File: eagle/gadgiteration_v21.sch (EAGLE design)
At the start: 56 parts, among them IC1 ATMEGA168P, J1 2.1MMJACK, U2 TPA2005D1DGNRQ1, X1 16.00MHz

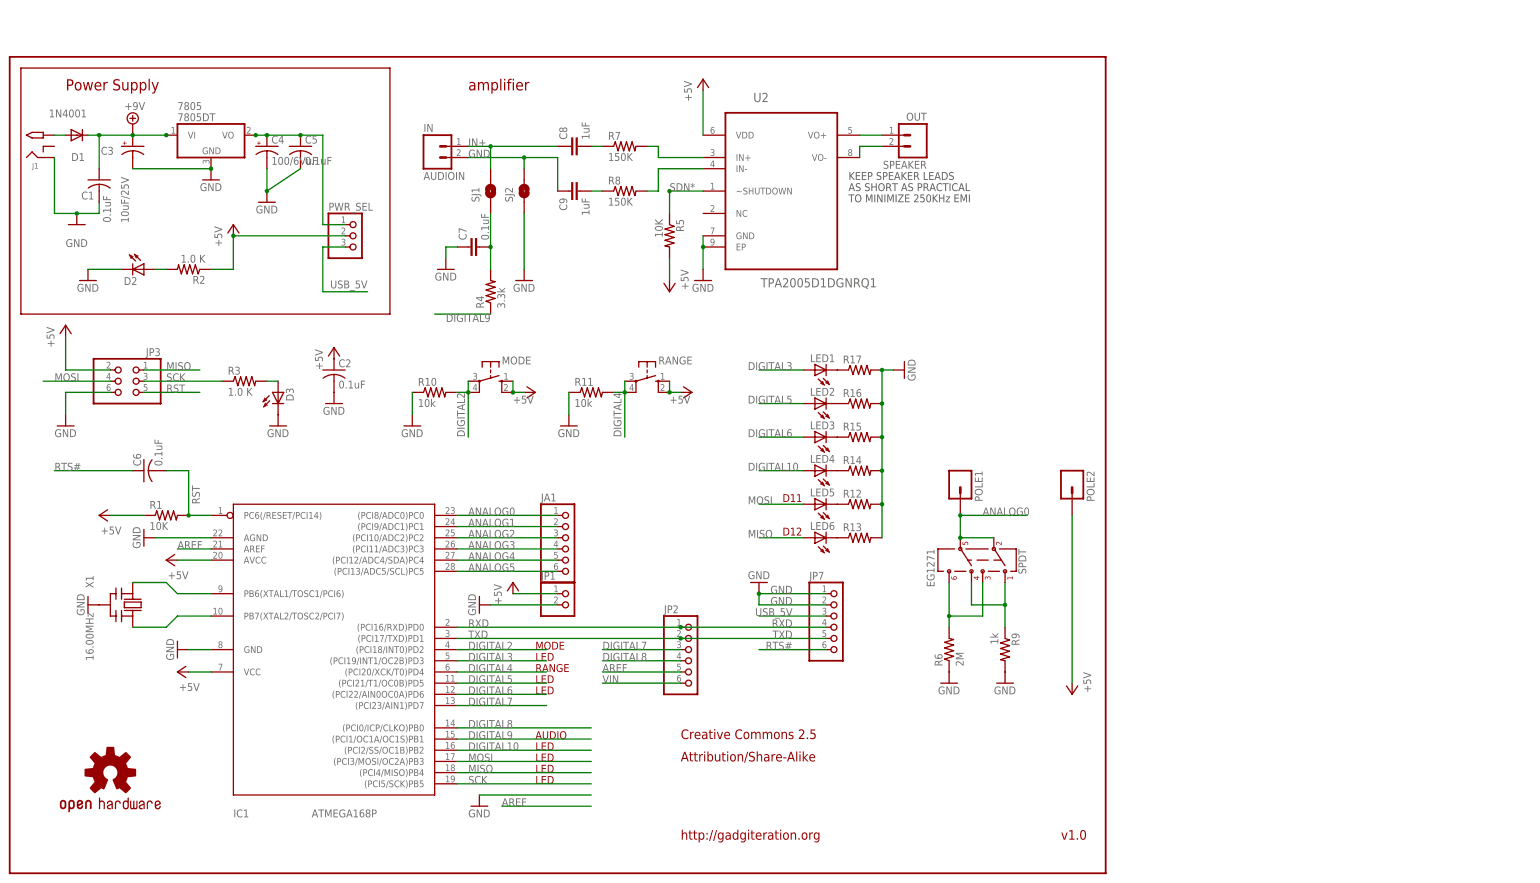
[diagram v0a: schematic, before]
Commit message: added v21 files, including readme and eagle files
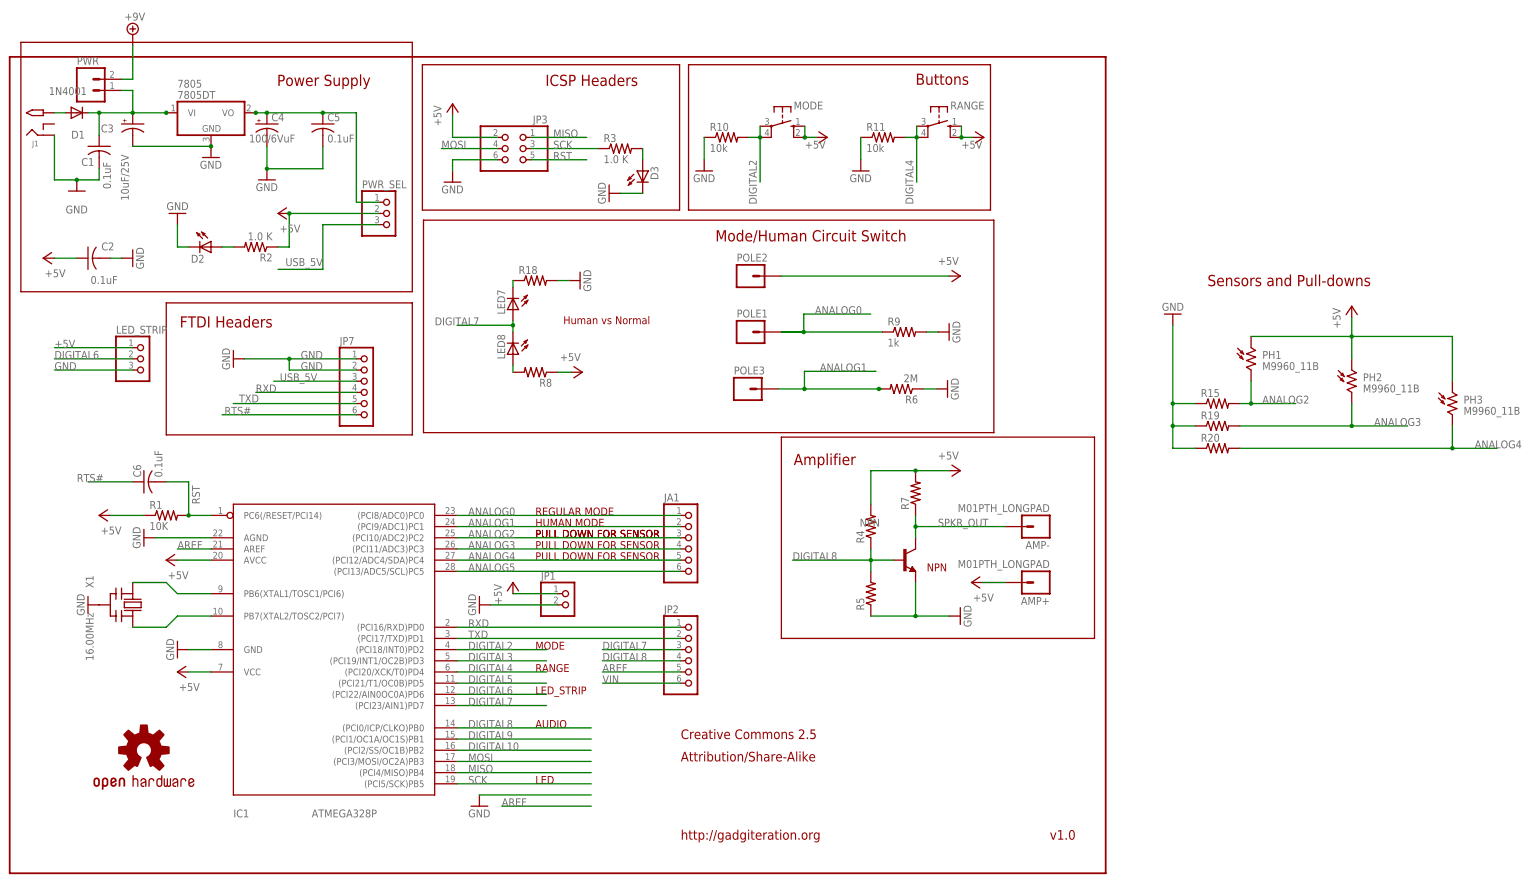
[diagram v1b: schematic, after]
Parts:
- removed AUDIOIN: IN, SparkFun:M02PTH
- removed C7: 0.1uF, SparkFun-Capacitors:CAPKIT
- removed C8, C9: 1uF, SparkFun:CAP1206
- removed LED1, LED2, LED3, LED4, LED5, LED6: (no value), led:LEDCHIPLED_1206
- removed R12, R13, R14, R16, R17: (no value), resistor:R-US_M0805
- removed SJ1, SJ2: SOLDERJUMPERTRACE, SparkFun-Passives:SOLDERJUMPERTRACE
- removed SPEAKER: OUT, SparkFun-Connectors:M02PTH3
- removed U$1: (no value), jms_SparkFun-Electromechanical:AYZ0202
- removed U2: TPA2005D1DGNRQ1, Texas Instruments_By_element14_Batch_1:TPA2005D1DGNRQ1
- added AMP+, AMP-, POLE3: M01PTH_LONGPAD, SparkFun-Connectors:M01PTH_LONGPAD
- added LED7, LED8: (no value), adafruit:LED3MM
- added LED_STRIP: (no value), pinhead:PINHD-1X3
- added NPN: (no value), transistor:-NPN-TO220V
- added PH1, PH2, PH3: M9960_11B, photo-elements:M9960_11B
- added PWR: (no value), SparkFun-Connectors:M02LOCK
- added R18, R19, R20: (no value), adafruit:R-US_0204/5
- IC1: value ATMEGA168P -> ATMEGA328P
- R1: device rcl-ez:R-US_0207/5V -> adafruit:R-US_0204/5
- R10, R11: device jms:R-US_R1206 -> adafruit:R-US_0204/5
- R15: device resistor:R-US_M0805 -> adafruit:R-US_0204/5
- R2, R3: device minimidi:R-US_0207/5V -> adafruit:R-US_0204/5
- R4: value 3.3k -> (none); device adafruit:R-US_M1206 -> adafruit:R-US_0204/5
- R5: value 10K -> (none)
- R7, R8: value 150K -> (none)
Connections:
- removed net IN+: AUDIOIN.1, C8.1, SJ1.2
- removed net IN+AMP: R7.2, U2.IN+
- removed net IN+_: C7.2, R4.2, SJ1.1
- removed net IN-AMP: R8.2, U2.IN-
- removed net N$10: LED6.C, R13.1
- removed net N$11: LED4.C, R14.1
- removed net N$12: LED3.C, R15.1
- removed net N$13: LED2.C, R16.1
- removed net N$14: LED1.C, R17.1
- removed net N$18: SPEAKER.1, U2.VO+
- removed net N$19: SPEAKER.2, U2.VO-
- removed net N$5: LED5.C, R12.1
- removed net N$8: R6.2, U$1.3, U$1.6
- removed net N$9: R9.1, U$1.1, U$1.4
- removed net SDN*: R5.1, U2.~SHUTDOWN
- new net +9V: PWR.2
- new net SPKR_OUT: AMP-.1, NPN.C, R7.1
- net +5V: now also AMP+.1, LED_STRIP.1, PH1.1, PH2.1, PH3.1, R4.2, R7.2, R8.1; no longer R5.2, U2.VDD
- net ANALOG0: now also R9.1; no longer U$1.2, U$1.5
- net ANALOG1: now also POLE3.1, R6.2
- net ANALOG2: now also PH1.2, R15.2
- net ANALOG3: now also PH2.2, R19.2
- net ANALOG4: now also PH3.2, R20.2
- net DIGITAL10: no longer LED4.A
- net DIGITAL3: no longer LED1.A
- net DIGITAL5: no longer LED2.A
- net DIGITAL6: now also LED_STRIP.2; no longer LED3.A
- net DIGITAL7: now also LED7.A, LED8.C
- net DIGITAL8: now also NPN.B, R4.1, R5.2
- net DIGITAL9: no longer R4.1
- net GND: now also LED_STRIP.3, NPN.E, R15.1, R18.2, R19.1, R20.1, R5.1; no longer AUDIOIN.2, C7.1, C9.1, R12.2, R13.2, R14.2, R15.2, R16.2, R17.2, SJ2.1, SJ2.2, U2.EP, U2.GND
- net MISO: no longer LED6.A
- net MOSI: no longer LED5.A
- net N$6: now also LED7.C, R18.1; no longer C8.2, R7.1
- net N$7: now also LED8.A, R8.2; no longer C9.2, R8.1
- net VIN: now also PWR.1
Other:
- note added: "Amplifier"
- note added: "Buttons"
- note added: "FTDI Headers"
- note added: "HUMAN MODE"
- note added: "Human vs Normal"
- note added: "ICSP Headers"
- note added: "LED_STRIP"
- note added: "Mode/Human Circuit Switch"
- note added: "NPN"
- note added: "PULL DOWN FOR SENSOR"
- note added: "REGULAR MODE"
- note added: "Sensors and Pull-downs"
- note removed: "AS SHORT AS PRACTICAL"
- note removed: "D11"
- note removed: "D12"
- note removed: "KEEP SPEAKER LEADS"
- note removed: "TO MINIMIZE 250KHz EMI"
- note removed: "amplifier"
- moved on the sheet: 7805, C1, C2, C3, C4, C5, C6, D1, D2, D3, J1, JA1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
